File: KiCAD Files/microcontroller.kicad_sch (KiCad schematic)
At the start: 25 parts, among them IC1 AZ1117IH-3.3TRG1, J3 61300511121, U2 STM32H7A3VGTx, Y1 LFXTAL010595

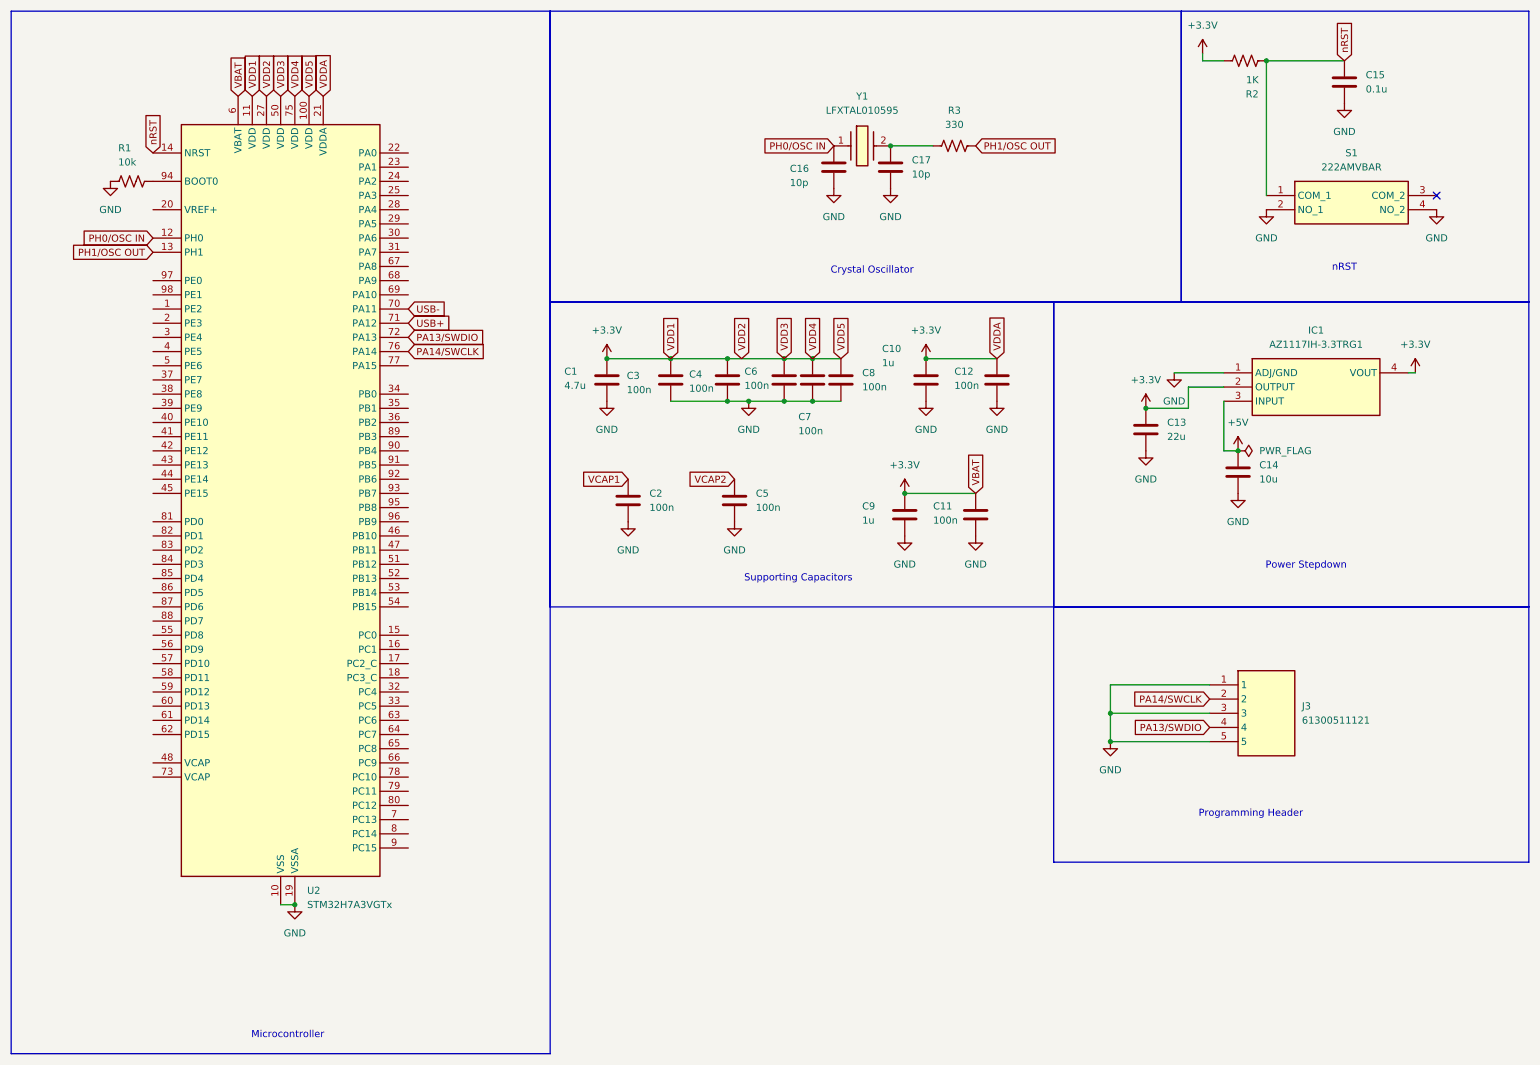
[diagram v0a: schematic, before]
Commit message: changed out microcontroller
Might add in a bit of debug circuitry + button leds will see tmmrw
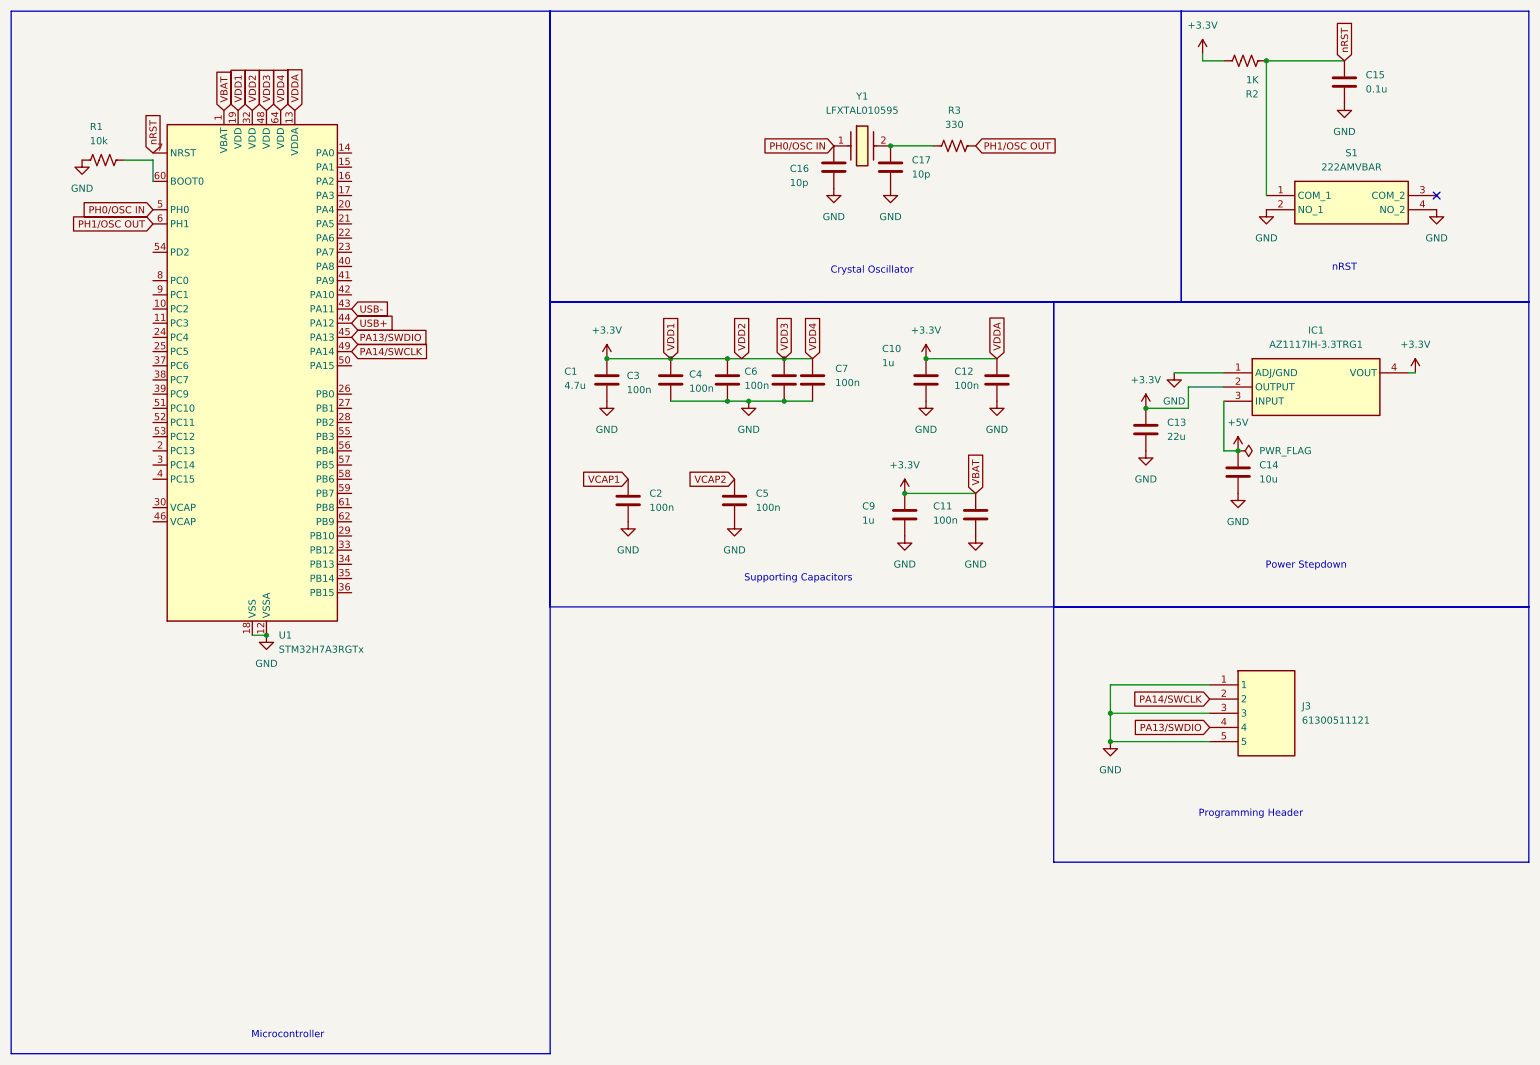
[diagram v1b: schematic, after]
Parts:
- removed C8: 100n, Capacitor_SMD:C_0805_2012Metric_Pad1.18x1.45mm_HandSolder, symbol CustomSymbols:C
- removed U2: STM32H7A3VGTx, Package_QFP:LQFP-100_14x14mm_P0.5mm, symbol MCU_ST_STM32H7:STM32H7A3VGTx
- added U1: STM32H7A3RGTx, Package_QFP:LQFP-64_10x10mm_P0.5mm, symbol MCU_ST_STM32H7:STM32H7A3RGTx
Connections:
- net +3.3V: now also U1.1 (VBAT), U1.13 (VDDA), U1.19 (VDD), U1.32 (VDD), U1.48 (VDD), U1.64 (VDD)
- net GND: now also U1.12 (VSSA), U1.18 (VSS), U1.31 (VSS), U1.47 (VSS), U1.63 (VSS)
- net PA13/SWDIO: now also U1.45 (PA13)
- net PA14/SWCLK: now also U1.49 (PA14)
- net PH0/OSC IN: now also U1.5 (PH0)
- net PH1/OSC OUT: now also U1.6 (PH1)
- net USB+: now also U1.44 (PA12)
- net USB-: now also U1.43 (PA11)
- net nRST: now also U1.7 (NRST)
- net at R1.1: now also U1.60 (BOOT0)
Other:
- moved on the sheet: R1

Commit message: improved PCB design and added debugging circuitry
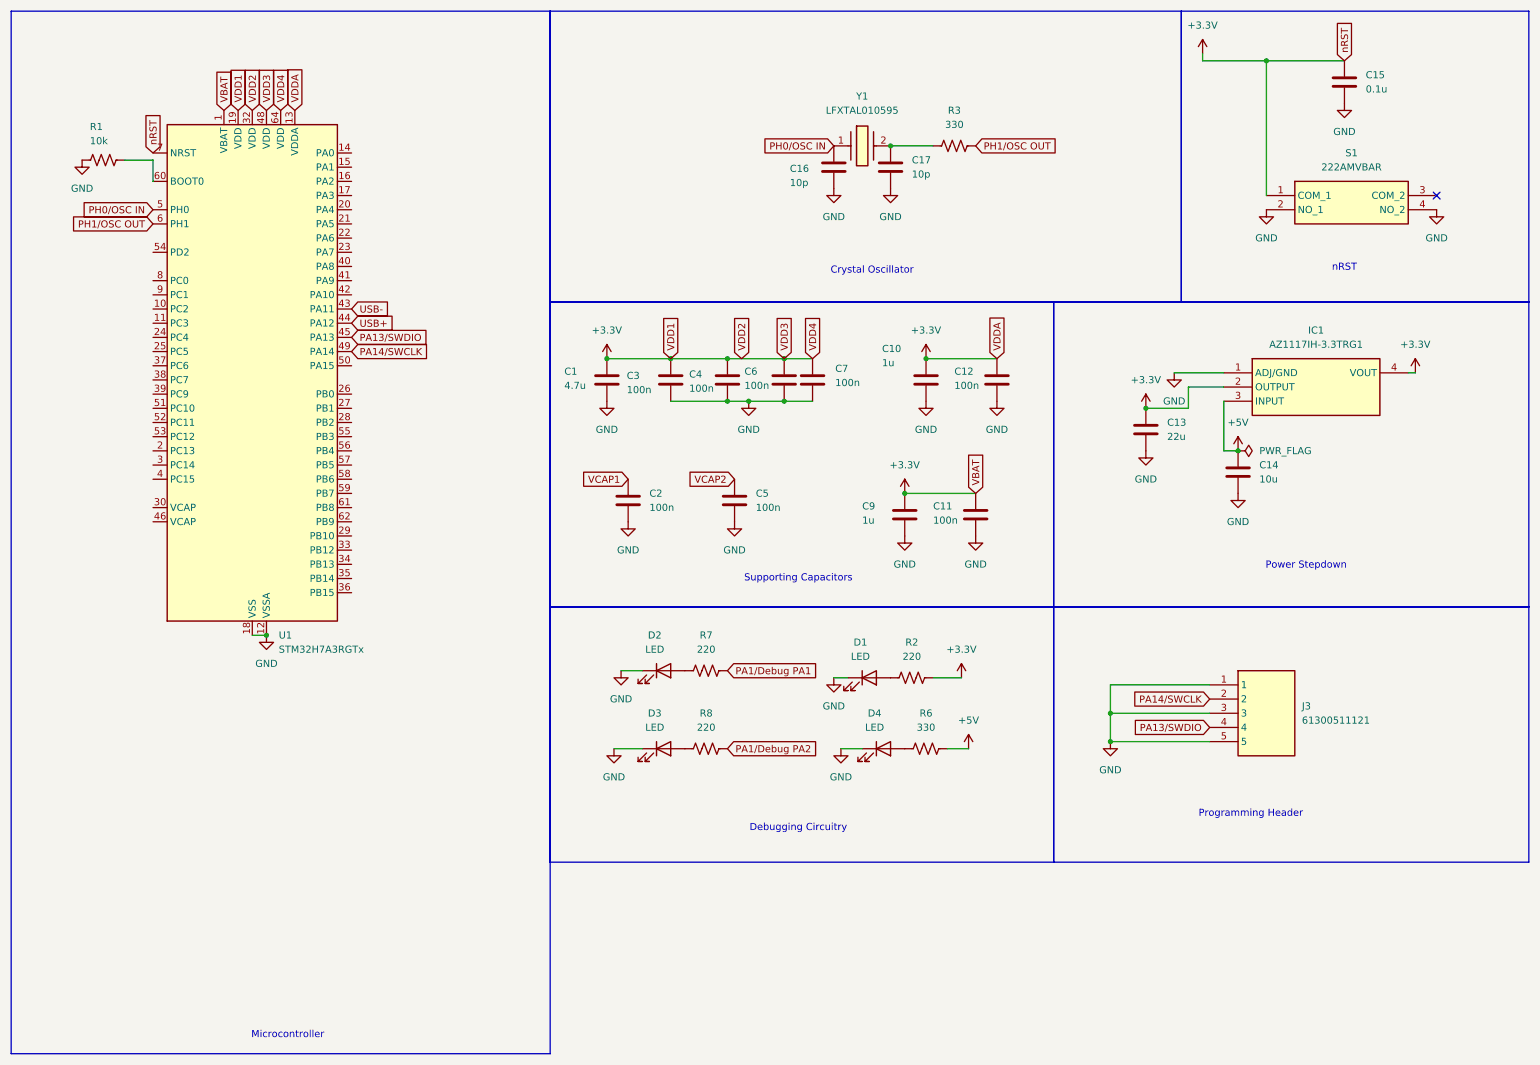
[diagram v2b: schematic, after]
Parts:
- removed R2: 1K, Resistor_SMD:R_0805_2012Metric_Pad1.20x1.40mm_HandSolder, symbol CustomSymbols:R_US
- added D1, D2, D3, D4: LED, LED_SMD:LED_0805_2012Metric_Pad1.15x1.40mm_HandSolder, symbol Device:LED
- added R2, R7, R8: 220, Resistor_SMD:R_0805_2012Metric_Pad1.20x1.40mm_HandSolder, symbol Device:R_US
- added R6: 330, Resistor_SMD:R_0805_2012Metric_Pad1.20x1.40mm_HandSolder, symbol Device:R_US
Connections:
- net nRST is gone; now on net +3.3V: C15.1, S1.1 (COM_1), U1.7 (NRST)
- net +3.3V: now also R2.1
- net +5V: now also R6.1
- net GND: now also D1.1 (K), D2.1 (K), D3.1 (K), D4.1 (K)
- new net: D2.2 (A), R7.2
- new net: D1.2 (A), R2.2
- new net: D4.2 (A), R6.2
- new net: D3.2 (A), R8.2
- new net PA1/Debug PA1: R7.1
- new net PA1/Debug PA2: R8.1
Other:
- note added: "Debugging Circuitry"

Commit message: finished pcb and diagram, need to double check before producing
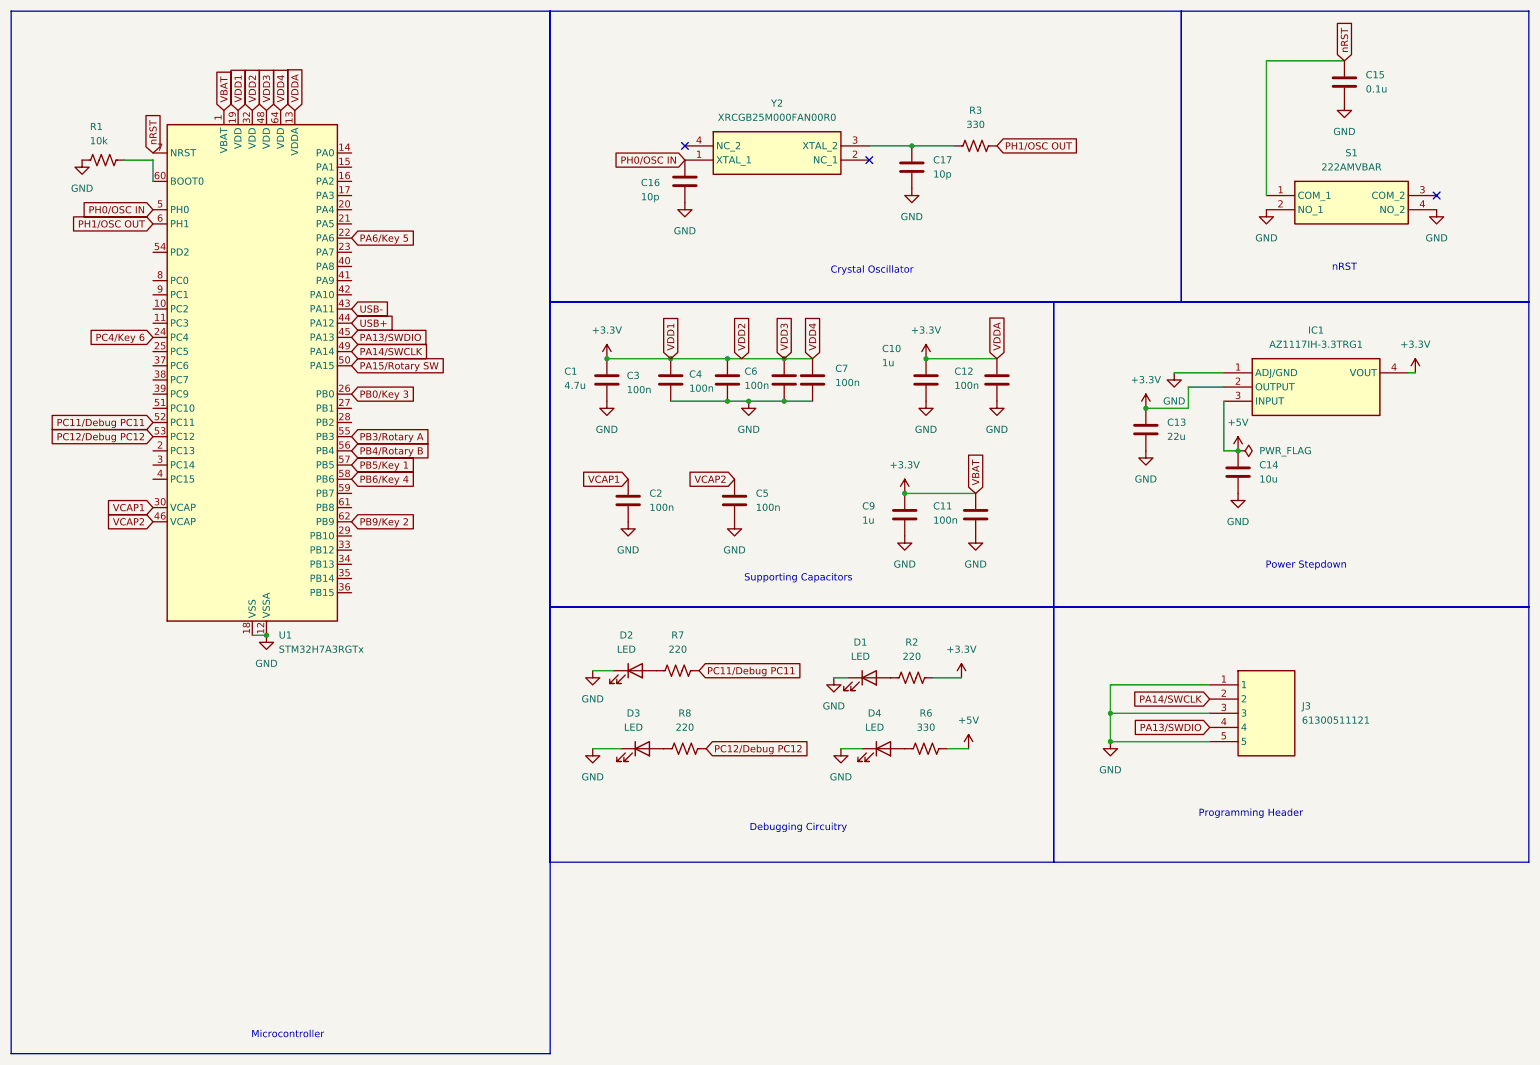
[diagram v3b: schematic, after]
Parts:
- removed Y1: LFXTAL010595, LFXTAL010595, symbol CustomSymbols:LFXTAL010595
- added Y2: XRCGB25M000FAN00R0, XRCGB, symbol CustomSymbols:XRCGB25M000FAN00R0
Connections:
- net PA1/Debug PA1 is gone; now on net PC11/Debug PC11: R7.1
- net PA1/Debug PA2 is gone; now on net PC12/Debug PC12: R8.1
- net +3.3V: no longer C15.1, S1.1 (COM_1), U1.7 (NRST)
- net PH0/OSC IN: now also Y2.1 (XTAL_1)
- net VCAP1: now also U1.30 (VCAP)
- net VCAP2: now also U1.46 (VCAP)
- net at C17.1, R3.1: now also Y2.3 (XTAL_2)
- net PA6/Key 5: now reaches U1.22 (PA6)
- net PC4/Key 6: now reaches U1.24 (PC4)
- net PB0/Key 3: now reaches U1.26 (PB0)
- net PA15/Rotary SW: now reaches U1.50 (PA15)
- net PC11/Debug PC11: now reaches U1.52 (PC11)
- net PC12/Debug PC12: now reaches U1.53 (PC12)
- net PB3/Rotary A: now reaches U1.55 (PB3)
- net PB4/Rotary B: now reaches U1.56 (PB4)
- net PB5/Key 1: now reaches U1.57 (PB5)
- net PB6/Key 4: now reaches U1.58 (PB6)
- net PB9/Key 2: now reaches U1.62 (PB9)
- new net nRST: C15.1, S1.1 (COM_1), U1.7 (NRST)
- no-connect marks 1 -> 3
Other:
- moved on the sheet: C16, C17, D2, D3, R3, R7, R8

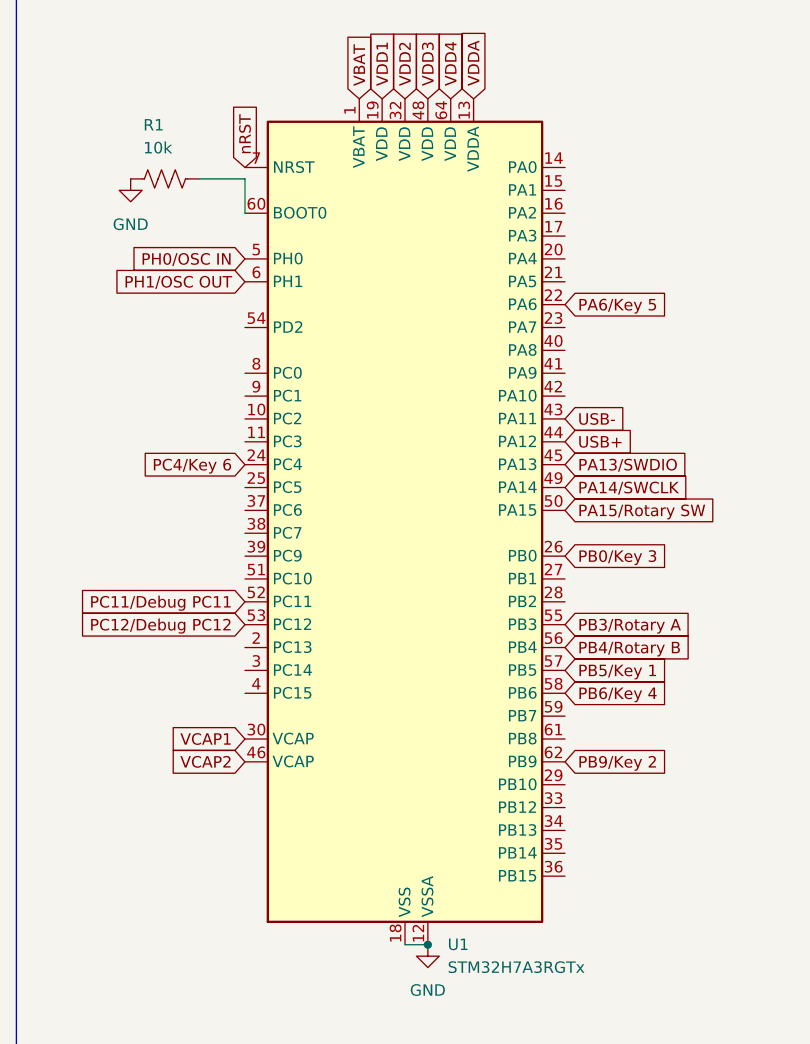
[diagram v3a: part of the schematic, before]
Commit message: tweaked 3d model + added drill files for jlc
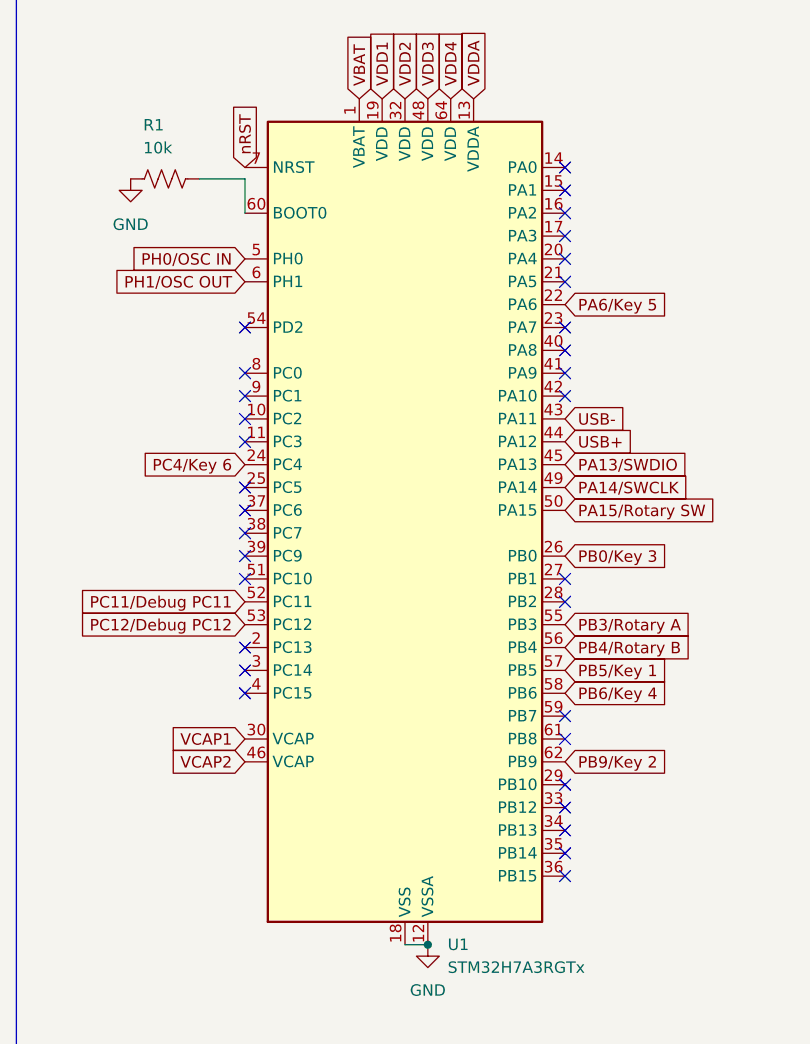
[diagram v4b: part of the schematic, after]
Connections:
- no-connect marks 3 -> 35
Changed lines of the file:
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@@
+	)
+	(no_connect
+		(at 73.66 86.36)
+	)
+	(no_connect
+		(at 38.1 78.74)
+	)
+	(no_connect
+		(at 73.66 83.82)
 	)
 	(no_connect
@@
 	)
 	(no_connect
+		(at 73.66 60.96)
+	)
+	(no_connect
+		(at 38.1 55.88)
+	)
+	(no_connect
+		(at 38.1 91.44)
+	)
+	(no_connect
+		(at 73.66 99.06)
+	)
+	(no_connect
+		(at 73.66 38.1)
+	)
+	(no_connect
+		(at 73.66 114.3)
+	)
+	(no_connect
+		(at 73.66 106.68)
+	)
+	(no_connect
+		(at 73.66 111.76)
+	)
+	(no_connect
+		(at 73.66 55.88)
+	)
+	(no_connect
+		(at 38.1 81.28)
+	)
+	(no_connect
+		(at 73.66 48.26)
+	)
+	(no_connect
+		(at 38.1 63.5)
+	)
+	(no_connect
+		(at 38.1 68.58)
+	)
+	(no_connect
+		(at 38.1 96.52)
+	)
+	(no_connect
+		(at 38.1 83.82)
+	)
+	(no_connect
+		(at 38.1 66.04)
+	)
+	(no_connect
+		(at 38.1 60.96)
+	)
+	(no_connect
+		(at 38.1 76.2)
+	)
+	(no_connect
+		(at 73.66 43.18)
+	)
+	(no_connect
+		(at 73.66 116.84)
+	)
+	(no_connect
+		(at 73.66 101.6)
+	)
+	(no_connect
+		(at 73.66 40.64)
+	)
+	(no_connect
+		(at 73.66 63.5)
+	)
+	(no_connect
+		(at 38.1 73.66)
+	)
+	(no_connect
+		(at 73.66 45.72)
+	)
+	(no_connect
+		(at 73.66 109.22)
+	)
+	(no_connect
+		(at 73.66 58.42)
+	)
+	(no_connect
+		(at 73.66 50.8)
+	)
+	(no_connect
+		(at 38.1 93.98)
+	)
+	(no_connect
